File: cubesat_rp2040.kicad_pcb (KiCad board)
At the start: 4 copper layers, 90.2 x 95.9 mm, 51 parts, among them J1 USB_C_Receptacle_USB2.0, J2 FTSH-105-01-L-DV-007, J5 Conn_01x02, SW1 SW_Push, U1 L7983, U3 RP2040, U4 W25Q128JVS

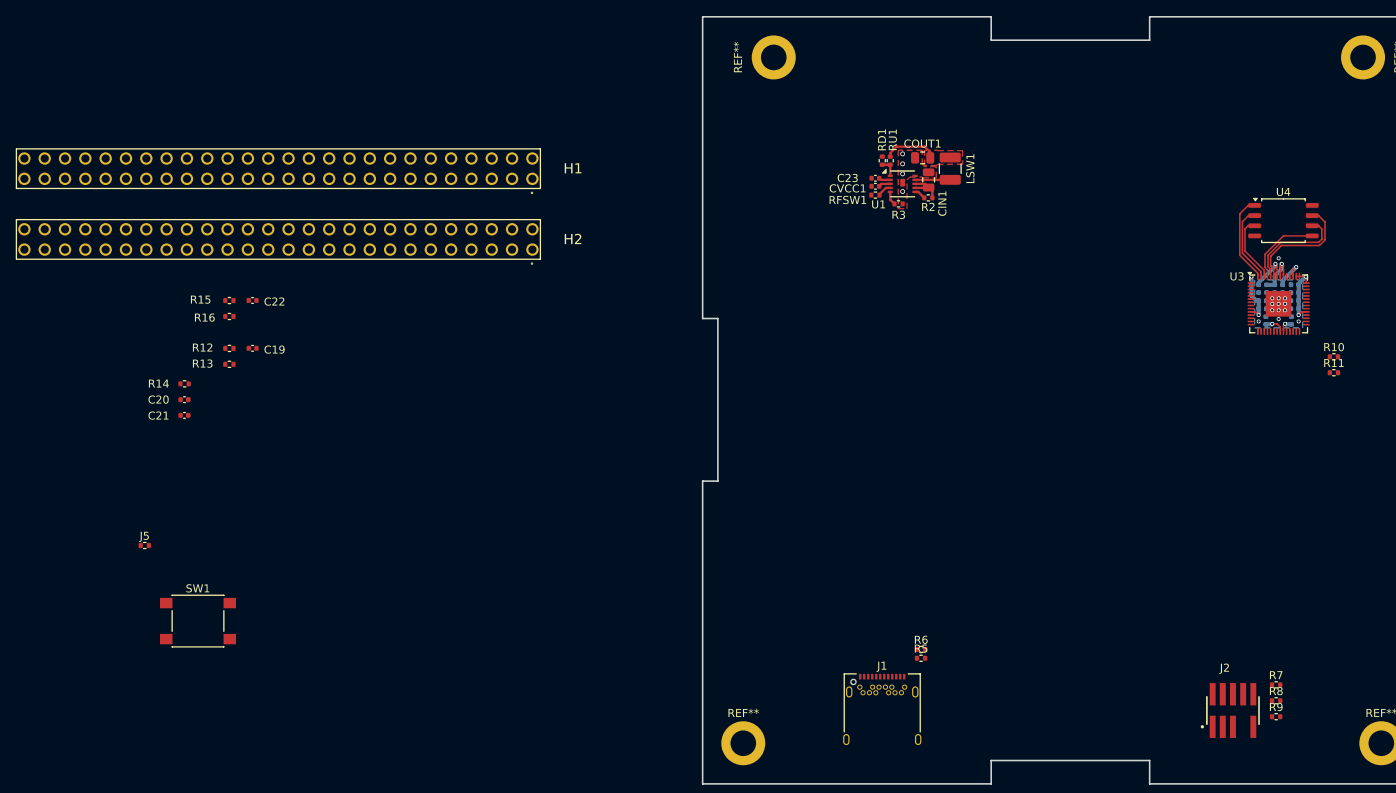
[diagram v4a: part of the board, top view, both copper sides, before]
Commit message: Update footprints, route more circuit blocks
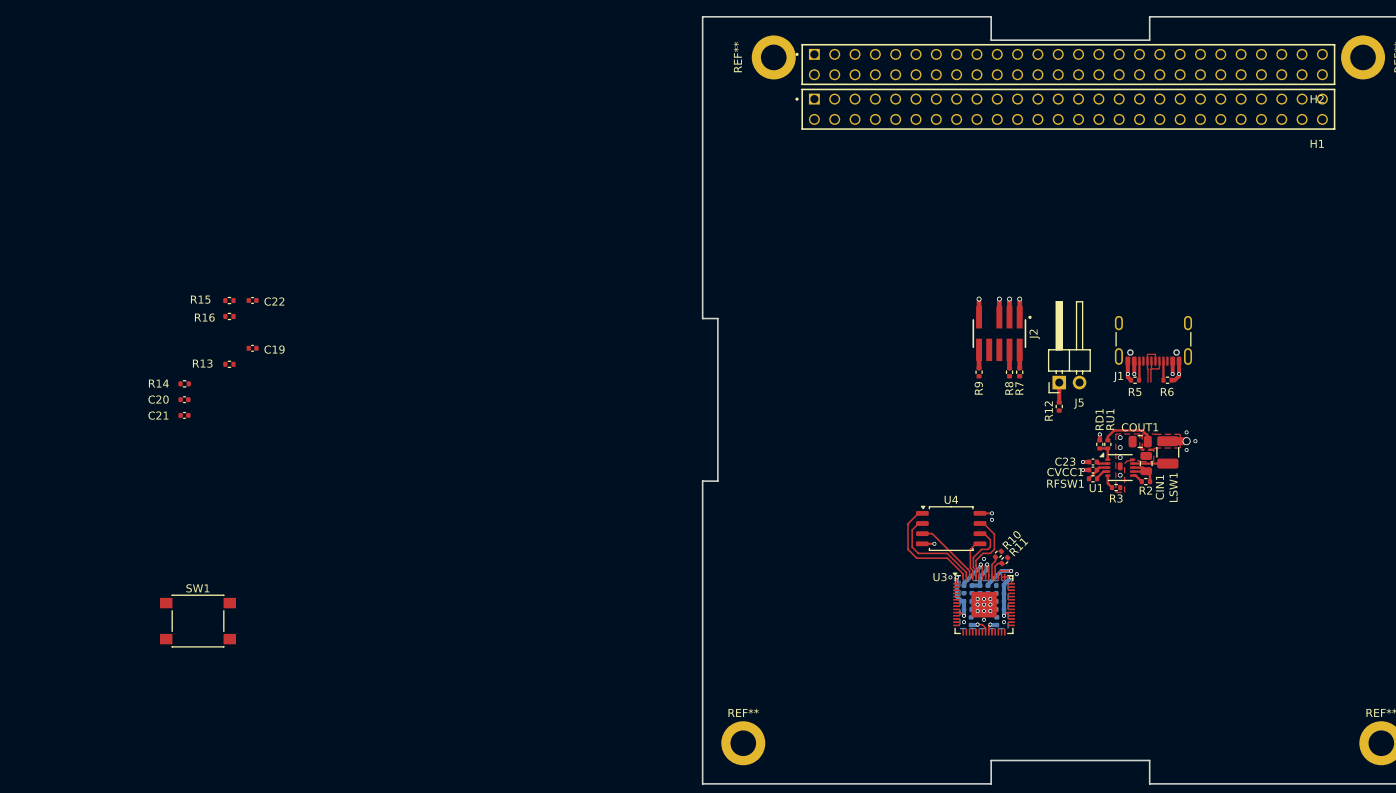
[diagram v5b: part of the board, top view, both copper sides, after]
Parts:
- H1, H2: footprint cubesat_rp2040:ESQ-126-Y-X-D -> cubesat_rp2040:SAMTEC_ESQ-126-39-G-D
- J1: footprint Connector_USB:USB_C_Receptacle_Amphenol_12401548E4-2A -> Connector_USB:USB_C_Receptacle_GCT_USB4105-xx-A_16P_TopMnt_Horizontal
- J5: footprint Resistor_SMD:R_0402_1005Metric -> Connector_PinHeader_2.54mm:PinHeader_1x02_P2.54mm_Horizontal
- R10, R11: value R -> 27R
- R12: value R -> 1k
- R13: value R -> 10k
- R5: value R -> R.1k
- R6: value R -> 5.1k
- moved J5 116.1 mm to (197.0, 102.2), turned to 90 degrees
- moved R12 104.0 mm to (197.0, 105.2), turned to 90 degrees
- moved J1 58.9 mm to (208.8, 95.9), turned to 180 degrees
- moved R9 56.9 mm to (187.0, 100.9), turned to -90 degrees
- moved U4 56.6 mm to (183.5, 120.5)
- moved J2 55.4 mm to (189.5, 96.1), turned to 180 degrees
- moved R8 52.9 mm to (190.8, 100.9), turned to 90 degrees
- moved C18 52.6 mm to (186.0, 132.1)
- moved C7 52.6 mm to (189.2, 132.1)
- moved C10 52.6 mm to (185.6, 129.6)
- moved C11 52.6 mm to (185.6, 130.6)
- moved C12 52.6 mm to (189.6, 130.6)
- moved C13 52.6 mm to (189.6, 129.6)
- moved C14 52.6 mm to (189.6, 128.6)
- moved C15 52.6 mm to (189.6, 127.6)
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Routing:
- net GND: track 0.00 -> 16.1 mm, vias 17 -> 32
- net +3V3: track 33.6 -> 39.7 mm, vias 6 -> 9
- net /RP2040/USB.D+: track 0.00 -> 5.34 mm
- net /Flash/QSPI.SCLK: track 13.0 -> 7.76 mm
- net /Flash/QSPI.SD3: track 14.5 -> 9.37 mm
- net /Flash/QSPI.SD0: track 9.74 -> 5.07 mm
- net /RP2040/USB.D-: track 0.00 -> 4.49 mm
- net /VBUS: track 5.10 -> 8.25 mm, vias 0 -> 2
- net /Flash/QSPI.~{SS}: track 11.0 -> 14.1 mm
- net /Flash/QSPI.SD1: track 9.64 -> 12.4 mm
- net Net-(U3-USB_DP): track 0.00 -> 2.68 mm
- net /Flash/~{USB_BOOT}: track 0.00 -> 2.48 mm
- net /USB Type-C connector/USB_CC2: track 0.00 -> 2.36 mm
- net /USB Type-C connector/USB_CC1: track 0.00 -> 2.34 mm
- net Net-(U3-USB_DM): track 0.00 -> 2.34 mm
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
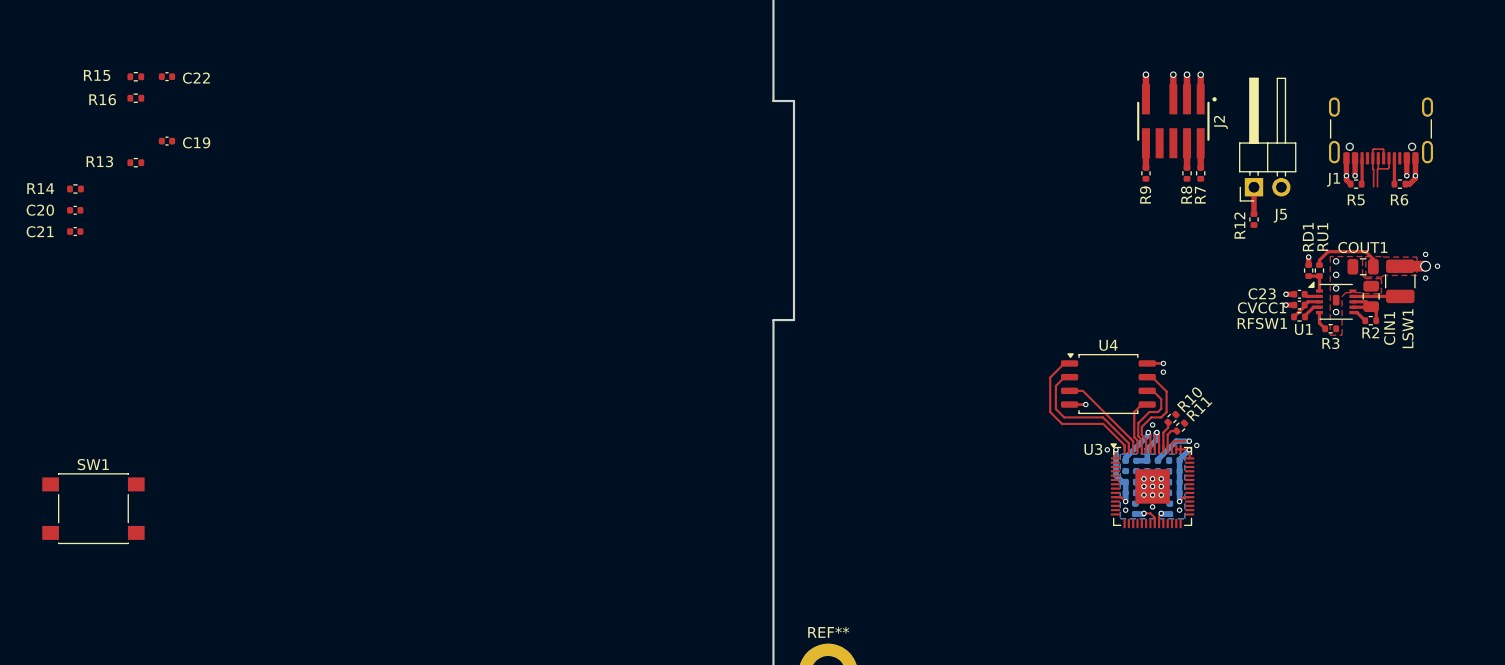
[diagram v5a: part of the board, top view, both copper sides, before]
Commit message: Update README, change footprints
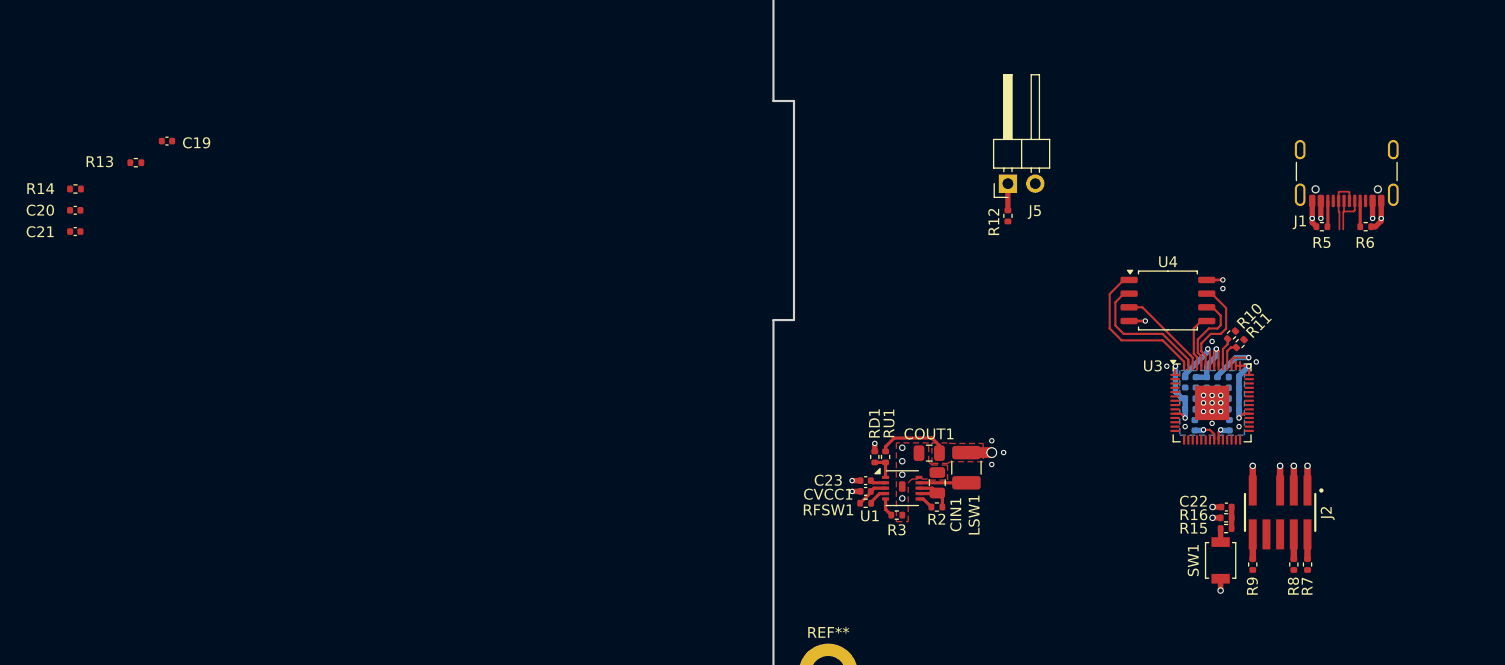
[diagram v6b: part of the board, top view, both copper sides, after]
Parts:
- SW1: footprint Button_Switch_SMD:SW_Push_1P1T_NO_6x6mm_H9.5mm -> Button_Switch_SMD:SW_SPST_B3U-1000P
- moved R15 109.5 mm to (194.4, 133.9), turned to 180 degrees
- moved R16 108.4 mm to (194.4, 132.9)
- moved C22 106.1 mm to (194.4, 131.9), turned to 180 degrees
- moved SW1 104.7 mm to (193.9, 136.8), turned to 90 degrees
- moved C23 43.8 mm to (160.9, 129.4)
- moved CIN1 43.8 mm to (167.6, 129.7)
- moved COUT1 43.8 mm to (166.8, 126.9)
- moved CVCC1 43.8 mm to (160.9, 130.4)
- moved RFSW1 43.8 mm to (160.9, 131.6)
- moved U1 43.8 mm to (164.3, 130.2)
- moved LSW1 43.8 mm to (170.3, 128.2)
- moved R2 43.8 mm to (167.6, 131.9)
- moved R3 43.8 mm to (163.8, 132.7)
- moved RD1 43.8 mm to (161.8, 127.2)
- moved RU1 43.8 mm to (162.8, 127.2)
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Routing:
- net /Debug/RUN: track 3.74 -> 5.74 mm
- net GND: track 16.1 -> 18.0 mm, vias 32 -> 34
- net Net-(R15-Pad2): track 0.00 -> 1.25 mm
- net +3V3: track 39.7 -> 40.5 mm, vias 9 -> 10

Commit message: Big update, bad commit messsage :)
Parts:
- removed C20, C21: C_Small, Capacitor_SMD:C_0402_1005Metric
- removed R14: R, Resistor_SMD:R_0402_1005Metric
- added C1001: 100n, cubesat_rp2040:C_0402_1005Metric, B.Cu at (167.2, 126.2)
- added C1002: 100n, cubesat_rp2040:C_0402_1005Metric, B.Cu at (170.5, 134.8)
- added C1003: 100n, cubesat_rp2040:C_0402_1005Metric, B.Cu at (175.8, 134.8)
- added C1004: 100n, cubesat_rp2040:C_0402_1005Metric, B.Cu at (177.8, 125.8)
- added C1005: 100n, cubesat_rp2040:C_0402_1005Metric, B.Cu at (169.5, 134.8)
- added C1006: 100n, cubesat_rp2040:C_0402_1005Metric, B.Cu at (172.8, 134.8)
- added C1007: 100n, cubesat_rp2040:C_0402_1005Metric, B.Cu at (177.8, 131.2)
- added C1008: 100n, cubesat_rp2040:C_0402_1005Metric, B.Cu at (177.8, 127.2)
- added C1009: 100n, cubesat_rp2040:C_0402_1005Metric, B.Cu at (174.2, 124.2)
- added C1010: 100n, cubesat_rp2040:C_0402_1005Metric, B.Cu at (170.8, 124.2)
- added C1011: 100n, cubesat_rp2040:C_0402_1005Metric, B.Cu at (169.2, 124.2)
- added C1012: 1u, cubesat_rp2040:C_0402_1005Metric, B.Cu at (167.8, 124.2)
- added C1013: 1u, cubesat_rp2040:C_0402_1005Metric, B.Cu at (177.2, 124.2)
- added C301: 100n, cubesat_rp2040:C_0402_1005Metric, F.Cu at (175.8, 142.3)
- added C302: 1n, cubesat_rp2040:C_0402_1005Metric, F.Cu at (175.8, 141.3)
- added C303: 10u, cubesat_rp2040:C_0402_1005Metric, B.Cu at (168.1, 141.7)
- added C803: 100n, cubesat_rp2040:C_0402_1005Metric, F.Cu at (221.0, 122.1)
- added C804: 10n, cubesat_rp2040:C_0402_1005Metric, F.Cu at (223.4, 122.1)
- added R1001: 90.9k 1%, cubesat_rp2040:R_0402_1005Metric, F.Cu at (164.2, 133.8)
- added R1002: 10k 1%, cubesat_rp2040:R_0402_1005Metric, F.Cu at (165.2, 133.8)
- added R1004: 4.7k, cubesat_rp2040:R_0402_1005Metric, F.Cu at (162.7, 130.2)
- added R1005: 4.7k, cubesat_rp2040:R_0402_1005Metric, F.Cu at (162.8, 124.8)
- added R1006: 4.7k, cubesat_rp2040:R_0402_1005Metric, F.Cu at (162.8, 125.8)
- added R1007: 4.7k, cubesat_rp2040:R_0402_1005Metric, F.Cu at (162.8, 126.8)
- added R1008: 4.7k, cubesat_rp2040:R_0402_1005Metric, F.Cu at (162.8, 127.8)
- added R305: 1M, cubesat_rp2040:R_0402_1005Metric, F.Cu at (175.8, 140.3)
- added R503: 0R, cubesat_rp2040:R_0402_1005Metric, F.Cu at (221.0, 120.1)
- added R802: 33R, cubesat_rp2040:R_0402_1005Metric, F.Cu at (221.0, 121.1)
- added R803: 10k, cubesat_rp2040:R_0402_1005Metric, F.Cu at (223.4, 121.1)
- added U1001: TUSB4041I, Package_QFP:HTQFP-64-1EP_10x10mm_P0.5mm_EP8x8mm_Mask4.4x4.4mm_ThermalVias, F.Cu at (172.5, 129.5)
- added U801: T6405 R24M0, cubesat_rp2040:Crystal_SMD_Rakon_3225-4Pin_3.2x2.5mm, F.Cu at (222.2, 124.4)
- C201: renamed from CVCC1; footprint Capacitor_SMD:C_0402_1005Metric -> cubesat_rp2040:C_0402_1005Metric
- C202: renamed from CIN1; footprint Capacitor_SMD:C_0805_2012Metric -> cubesat_rp2040:C_0402_1005Metric
- C203: renamed from C23; footprint Capacitor_SMD:C_0402_1005Metric -> cubesat_rp2040:C_0402_1005Metric
- C204: renamed from COUT1; footprint Capacitor_SMD:C_0805_2012Metric -> cubesat_rp2040:C_0402_1005Metric
- C501: renamed from C7; footprint Capacitor_SMD:C_0402_1005Metric -> cubesat_rp2040:C_0402_1005Metric
- C502: renamed from C8; footprint Capacitor_SMD:C_0402_1005Metric -> cubesat_rp2040:C_0402_1005Metric
- C503: renamed from C9; footprint Capacitor_SMD:C_0402_1005Metric -> cubesat_rp2040:C_0402_1005Metric
- C504: renamed from C10; footprint Capacitor_SMD:C_0402_1005Metric -> cubesat_rp2040:C_0402_1005Metric
- C505: renamed from C11; footprint Capacitor_SMD:C_0402_1005Metric -> cubesat_rp2040:C_0402_1005Metric
- C506: renamed from C12; footprint Capacitor_SMD:C_0402_1005Metric -> cubesat_rp2040:C_0402_1005Metric
- C507: renamed from C13; footprint Capacitor_SMD:C_0402_1005Metric -> cubesat_rp2040:C_0402_1005Metric
- C508: renamed from C14; footprint Capacitor_SMD:C_0402_1005Metric -> cubesat_rp2040:C_0402_1005Metric
- C509: renamed from C15; footprint Capacitor_SMD:C_0402_1005Metric -> cubesat_rp2040:C_0402_1005Metric
- C510: renamed from C16; footprint Capacitor_SMD:C_0402_1005Metric -> cubesat_rp2040:C_0402_1005Metric
- C511: renamed from C17; footprint Capacitor_SMD:C_0402_1005Metric -> cubesat_rp2040:C_0402_1005Metric
- C512: renamed from C18; footprint Capacitor_SMD:C_0402_1005Metric -> cubesat_rp2040:C_0402_1005Metric
- C701: renamed from C19; footprint Capacitor_SMD:C_0402_1005Metric -> cubesat_rp2040:C_0402_1005Metric
- C901: renamed from C22; value C_Small -> C; footprint Capacitor_SMD:C_0402_1005Metric -> cubesat_rp2040:C_0402_1005Metric
- R201: renamed from RFSW1; footprint Resistor_SMD:R_0402_1005Metric -> cubesat_rp2040:R_0402_1005Metric
- R202: renamed from R3; footprint Resistor_SMD:R_0402_1005Metric -> cubesat_rp2040:R_0402_1005Metric
- R203: renamed from R2; footprint Resistor_SMD:R_0402_1005Metric -> cubesat_rp2040:R_0402_1005Metric
- R204: renamed from RU1; footprint Resistor_SMD:R_0402_1005Metric -> cubesat_rp2040:R_0402_1005Metric
- R205: renamed from RD1; footprint Resistor_SMD:R_0402_1005Metric -> cubesat_rp2040:R_0402_1005Metric
- R301: renamed from R5; value R.1k -> 5.1k 10%; footprint Resistor_SMD:R_0402_1005Metric -> cubesat_rp2040:R_0402_1005Metric
- R302: renamed from R6; value 5.1k -> 5.1k 10%; footprint Resistor_SMD:R_0402_1005Metric -> cubesat_rp2040:R_0402_1005Metric
- R401: renamed from R7; footprint Resistor_SMD:R_0402_1005Metric -> cubesat_rp2040:R_0402_1005Metric
- R402: renamed from R8; footprint Resistor_SMD:R_0402_1005Metric -> cubesat_rp2040:R_0402_1005Metric
- R403: renamed from R9; footprint Resistor_SMD:R_0402_1005Metric -> cubesat_rp2040:R_0402_1005Metric
- R501: renamed from R10; footprint Resistor_SMD:R_0402_1005Metric -> cubesat_rp2040:R_0402_1005Metric
- R502: renamed from R11; footprint Resistor_SMD:R_0402_1005Metric -> cubesat_rp2040:R_0402_1005Metric
- R701: renamed from R12; footprint Resistor_SMD:R_0402_1005Metric -> cubesat_rp2040:R_0402_1005Metric
- R702: renamed from R13; footprint Resistor_SMD:R_0402_1005Metric -> cubesat_rp2040:R_0402_1005Metric
- R901: renamed from R15; footprint Resistor_SMD:R_0402_1005Metric -> cubesat_rp2040:R_0402_1005Metric
- R902: renamed from R16; footprint Resistor_SMD:R_0402_1005Metric -> cubesat_rp2040:R_0402_1005Metric
- moved C701 127.5 mm to (223.5, 103.6), turned to -90 degrees
- moved R702 122.2 mm to (215.5, 101.5), turned to 180 degrees
- moved C202 78.7 mm to (232.2, 84.8)
- moved C204 78.7 mm to (231.5, 82.0)
- moved R201 78.7 mm to (225.6, 86.7)
- moved R203 78.7 mm to (232.2, 87.0)
- moved U201 78.7 mm to (229.0, 85.3)
- moved C201 78.7 mm to (225.6, 85.6)
- moved C203 78.7 mm to (225.6, 84.6)
- moved R202 78.7 mm to (228.5, 87.8)
- moved L201 78.7 mm to (234.9, 83.4)
- moved R204 78.7 mm to (227.4, 82.4)
- moved R205 78.7 mm to (226.4, 82.4)
- moved J301 59.2 mm to (171.0, 147.8), turned to 0 degrees
- moved R302 52.3 mm to (169.2, 141.7), turned to 180 degrees
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- renumbered H1 to H601, H2 to H602, J1 to J301, J2 to J401, J5 to J701, LSW1 to L201, SW1 to SW901, U1 to U201, U3 to U501, U4 to U701
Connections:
- net /Debug/RUN renamed /Debug/~{RESET}
- net /Debug/SWDCLK renamed /Debug/SWCLK
- net /Power/FSW renamed /VBUS to 3V3/FSW
- net /Power/VCC renamed /VBUS to 3V3/VCC
- net /USB Type-C connector/USB_CC1 renamed /USB Type C connector/USB_UP.CC1
- net /USB Type-C connector/USB_CC2 renamed /USB Type C connector/USB_UP.CC2
- J301 pad A4: /VBUS -> /USB 2.0 Hub/VBUS
- J301 pad A6: /RP2040/USB.D+ -> /USB 2.0 Hub/USB_UP.D+
- J301 pad A7: /RP2040/USB.D- -> /USB 2.0 Hub/USB_UP.D-
- J301 pad A9: /VBUS -> /USB 2.0 Hub/VBUS
- J301 pad B4: /VBUS -> /USB 2.0 Hub/VBUS
- J301 pad B6: /RP2040/USB.D+ -> /USB 2.0 Hub/USB_UP.D+
- J301 pad B7: /RP2040/USB.D- -> /USB 2.0 Hub/USB_UP.D-
- J301 pad B9: /VBUS -> /USB 2.0 Hub/VBUS
- J301 pad S1: GND -> Earth
- U501 pad 19: GND -> Net-(U501-TESTEN)
- U501 pad 20: /Crystal oscillator/XIN -> /Oscillator/F_{out}
- U501 pad 21: /Crystal oscillator/XOUT -> unconnected-(U501-XOUT-Pad21)
- U501 pad 38: unconnected-(U3-GPIO26_ADC0-Pad38) -> /RP2040/ADC0
- U501 pad 39: unconnected-(U3-GPIO27_ADC1-Pad39) -> /RP2040/ADC1
- U501 pad 40: unconnected-(U3-GPIO28_ADC2-Pad40) -> /RP2040/ADC2
- U501 pad 41: unconnected-(U3-GPIO29_ADC3-Pad41) -> /RP2040/ADC3
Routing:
- net +1V1: track 12.9 -> 44.9 mm, vias 3 -> 10
- net +3V3: track 40.5 -> 70.8 mm, vias 10 -> 17
- net /Debug/SWCLK: track 2.28 -> 20.0 mm
- net /Debug/SWDIO: track 2.28 -> 19.3 mm
- net GND: track 18.0 -> 33.8 mm, vias 34 -> 59
- net /USB 2.0 Hub/USB_UP.D-: track 0.00 -> 12.5 mm, vias 0 -> 2
- net /USB 2.0 Hub/USB_UP.D+: track 0.00 -> 12.5 mm, vias 0 -> 2
- net /USB 2.0 Hub/PWRCTL3/BATEN3: track 0.00 -> 5.88 mm
- net /RP2040/USB.D+: track 5.34 -> 0.00 mm
- net /Oscillator/F_{out}: track 0.00 -> 4.99 mm
- net /USB 2.0 Hub/VBUS: track 0.00 -> 4.97 mm, vias 0 -> 3
- net /RP2040/USB.D-: track 4.49 -> 0.00 mm
- net Earth: track 0.00 -> 4.43 mm
- net /USB 2.0 Hub/PWRCTL2/BATEN2: track 0.00 -> 3.75 mm
- net /USB 2.0 Hub/PWRCTL1/BATEN1: track 0.00 -> 3.75 mm
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- added copper zone on B.Cu, net +3V3
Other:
- outline, holes or cut-outs redrawn
